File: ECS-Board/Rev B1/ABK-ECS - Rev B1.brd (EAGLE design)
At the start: 100 x 100 mm, 298 parts, among them J1 USB-B-S-RA, J10 FTSH-105-01-L-DV-NOPASTE, J11 22-05-7028-02, J12 RB1-125BAG1A, J13 22-05-7068-06, J14 22-05-7048-04, J15 22-05-7048-04, J16 22-05-7048-04, J2 MSTBA2, J3 22-05-7068-06, J5 22-05-7068-06, J6 22-05-7068-06, J7 22-05-7068-06, J8 22-05-7028-02, J9 FTSH-103-01-L-DV-NOPASTE, SW1 B3FS-1015, SW2 B3FS-1015, T1 MMBT2907ALT3, T10 MMBT2222AL, T11 IRLML5103TRPBF, T12 MMBT2222AL, T13 IRLML5103TRPBF, T14 IRLML5103TRPBF, T15 IRLML5103TRPBF, T16 IRLML5103TRPBF, T17 MMBT2222AL, T18 MMBT2222AL, T19 MMBT2222AL, T2 EXMACHINA-LOGO-NAME, T20 MMBT2222AL, T3 IRLML5103TRPBF, T4 IRLML5103TRPBF, T5 IRLML5103TRPBF, T6 IRLML5103TRPBF, T7 MMBT2222AL, T8 MMBT2222AL, T9 MMBT2222AL, U1 AT24C512C-SSHM-B, U10 SN74LVC2G17DBVR, U2 LPC1768FBD100, U3 LT3686HDDPBF, U4 LT3686HDDPBF, U5 CD4050BD, U6 CD4050BD, U7 DP83848JSQ/NOPB, U9 SN74LVC2G17DBVR, X1 FC-135, X2 ASE-12, X3 3000, X4 ASE_50

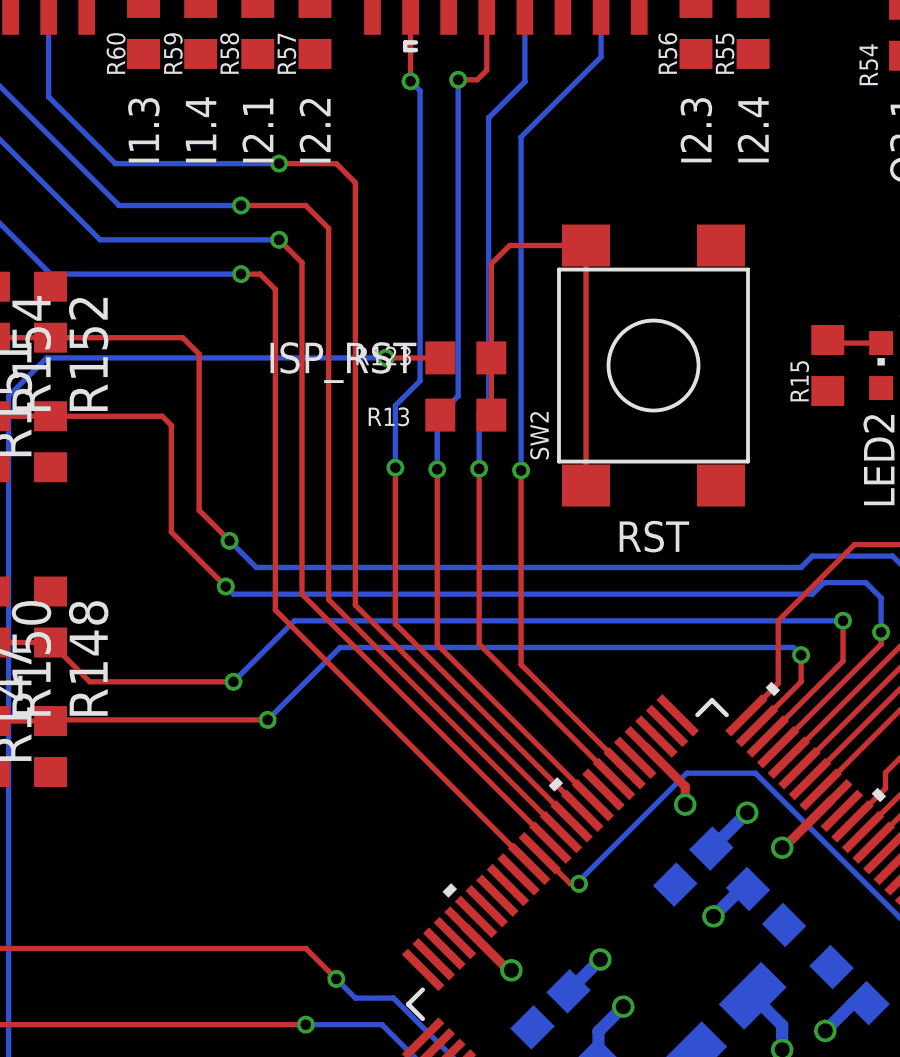
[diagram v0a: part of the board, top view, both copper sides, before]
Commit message: Re-Map MCU output signal
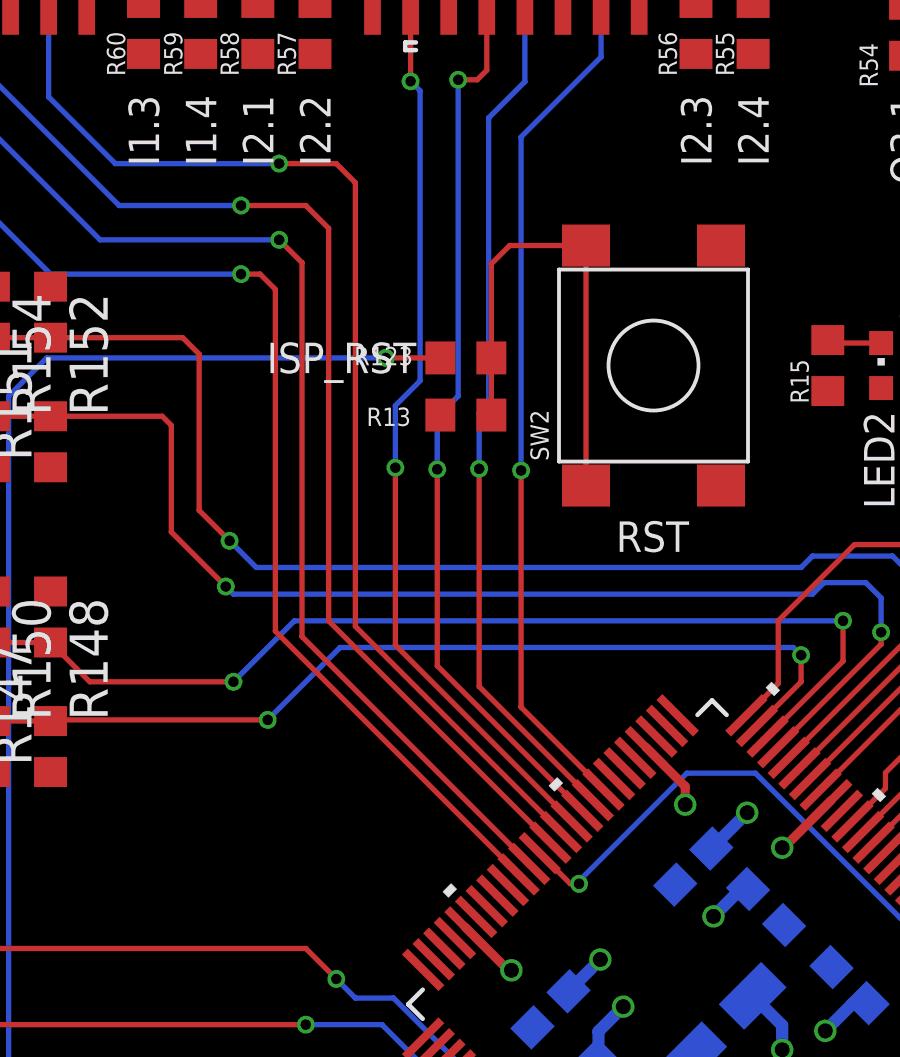
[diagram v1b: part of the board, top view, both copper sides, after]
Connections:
- net INPUT1.1_MCU: now also U2.66; no longer U2.65
- net INPUT1.2_MCU: now also U2.65; no longer U2.63
- net INPUT1.3_MCU: now also U2.63; no longer U2.62
- net INPUT1.4_MCU: now also U2.62; no longer U2.61
- net INPUT2.1_MCU: now also U2.60; no longer U2.59
- net INPUT2.2_MCU: now also U2.61; no longer U2.60
- net INPUT2.3_MCU: now also U2.59; no longer U2.57
- net INPUT2.4_MCU: now also U2.58; no longer U2.56
- net ONBOARD_LED1: now also U2.57
- net ONBOARD_LED2: now also U2.56

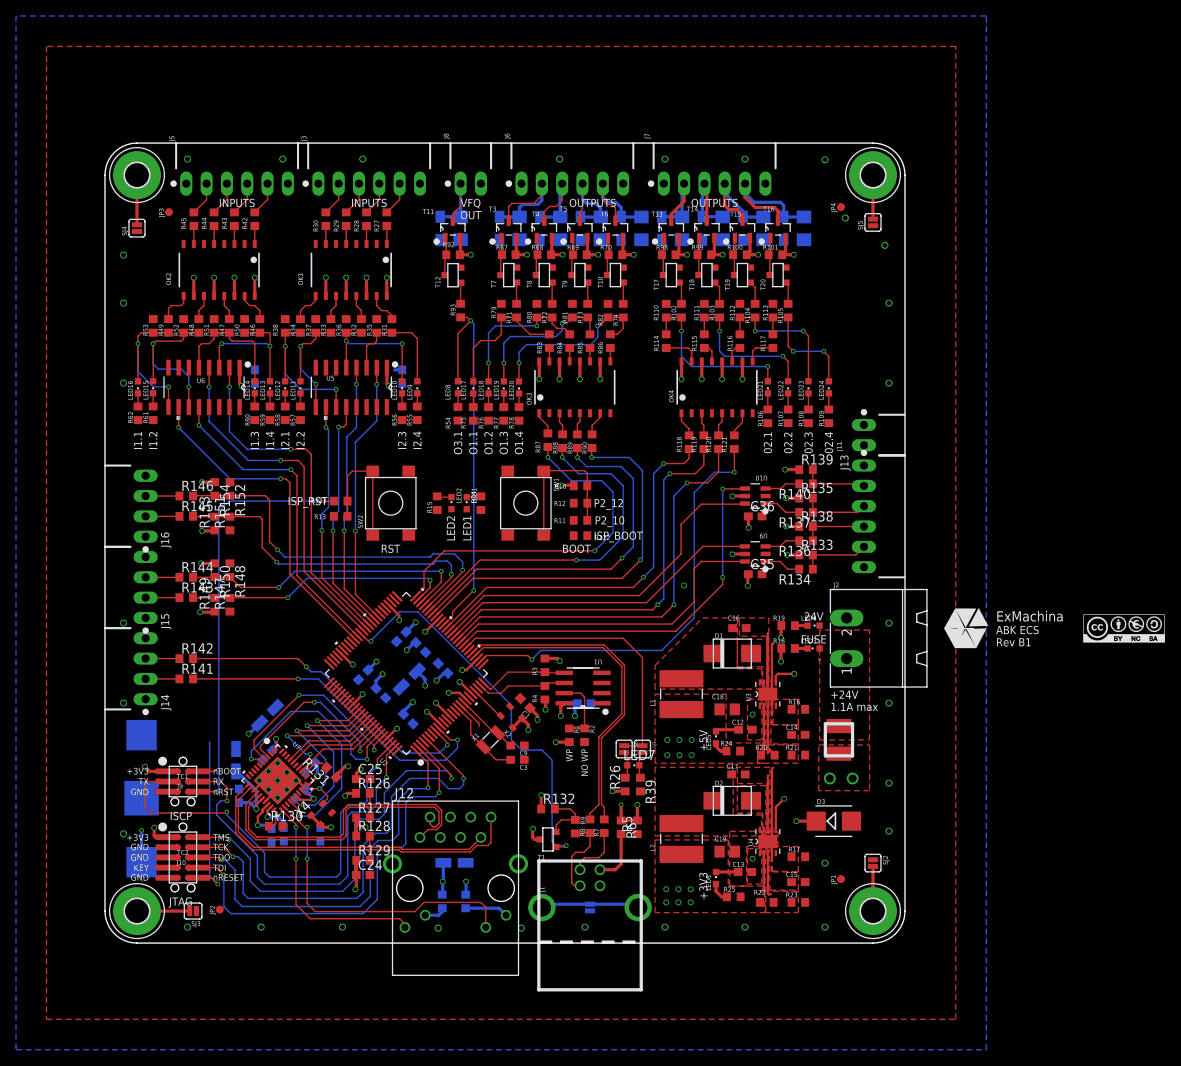
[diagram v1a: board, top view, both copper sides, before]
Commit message: Move RTC battery holder and route VBAT, Boot signals and Leds signals
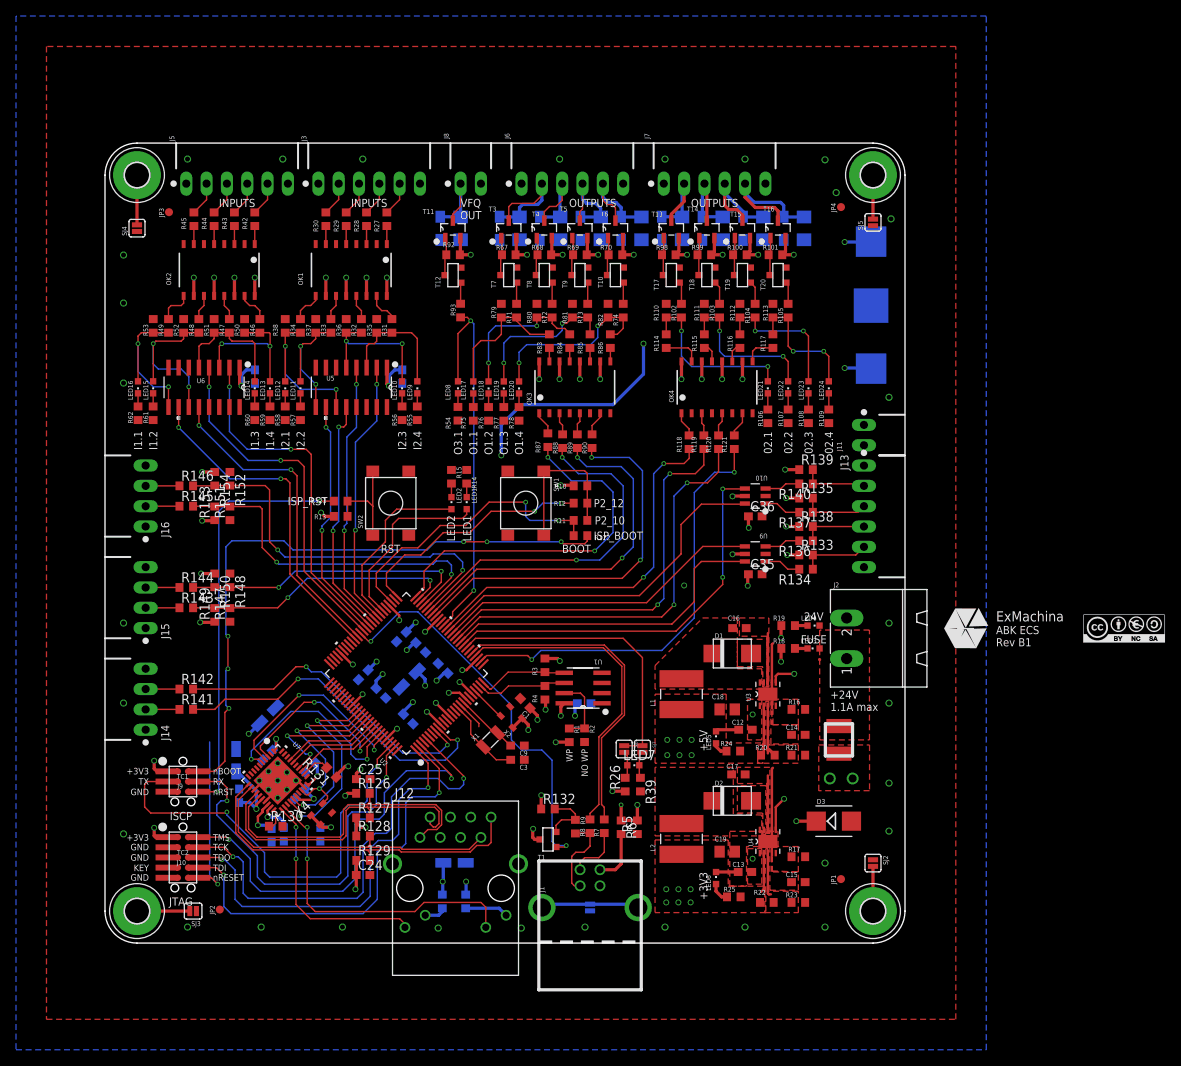
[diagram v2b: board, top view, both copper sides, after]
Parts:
- moved X3 110.0 mm to (95.8, 79.7), turned to 90 degrees
- moved R141 3.81 mm to (10.2, 29.2)
- moved R142 3.81 mm to (10.2, 31.8)
- moved J14 3.81 mm to (5.08, 30.5)
- moved R14 3.75 mm to (45.2, 58.3), turned to 90 degrees
- moved R15 3.75 mm to (43.3, 58.3), turned to 90 degrees
- moved J15 1.27 mm to (5.08, 43.2)
- moved J16 1.27 mm to (5.08, 55.9)
- moved R143 1.27 mm to (10.2, 41.9)
- moved R148 1.27 mm to (15.6, 45.3)
- moved R150 1.27 mm to (13.7, 45.3)
- moved R152 1.27 mm to (15.6, 58.0)
- moved R154 1.27 mm to (13.7, 58.0)
- moved R144 1.27 mm to (10.2, 44.5)
- moved R145 1.27 mm to (10.2, 54.6)
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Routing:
- net VBAT+: track 6.55 -> 113.8 mm, vias 2 -> 5
- net !ISP_BOOT: track 3.87 -> 79.8 mm, vias 0 -> 6
- net BOOT_SELECT_P2_10: track 0.00 -> 36.6 mm, vias 0 -> 2
- net BOOT_SELECT_P2_12: track 0.00 -> 30.5 mm, vias 0 -> 2
- net ONBOARD_LED2: track 0.00 -> 23.1 mm
- net ONBOARD_LED1: track 0.00 -> 22.6 mm
- net +3V3: track 121.3 -> 128.4 mm, vias 56 -> 57
- net !RESET: track 42.3 -> 39.2 mm
- net ADC2: track 42.0 -> 43.5 mm
- net UART_TX: track 48.1 -> 49.3 mm
- net UART_RX: track 43.6 -> 44.9 mm
- net ADC1: track 39.5 -> 40.2 mm
- net I2C_SDA: track 37.3 -> 36.8 mm
- net I2C_SCL: track 33.7 -> 34.3 mm
- net GND: vias 41 -> 40

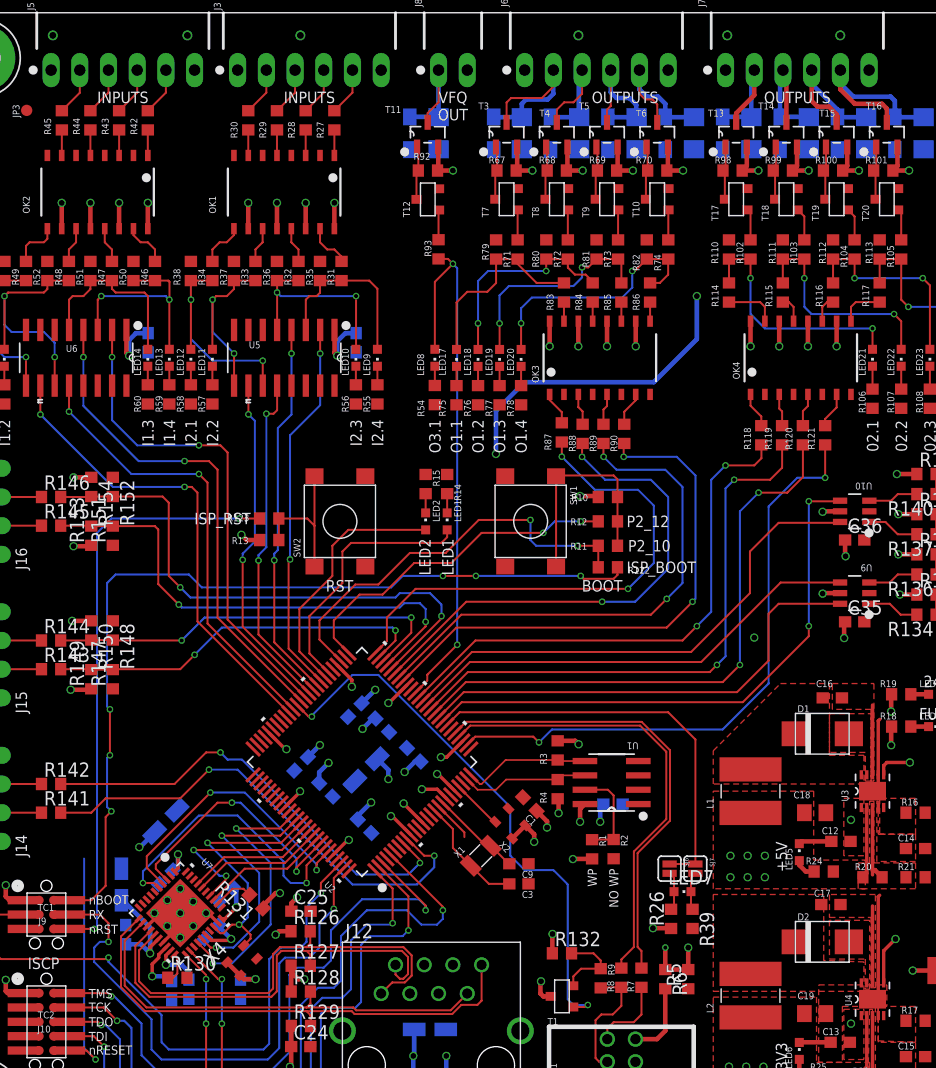
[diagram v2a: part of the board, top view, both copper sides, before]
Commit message: Route Reset and all airwire
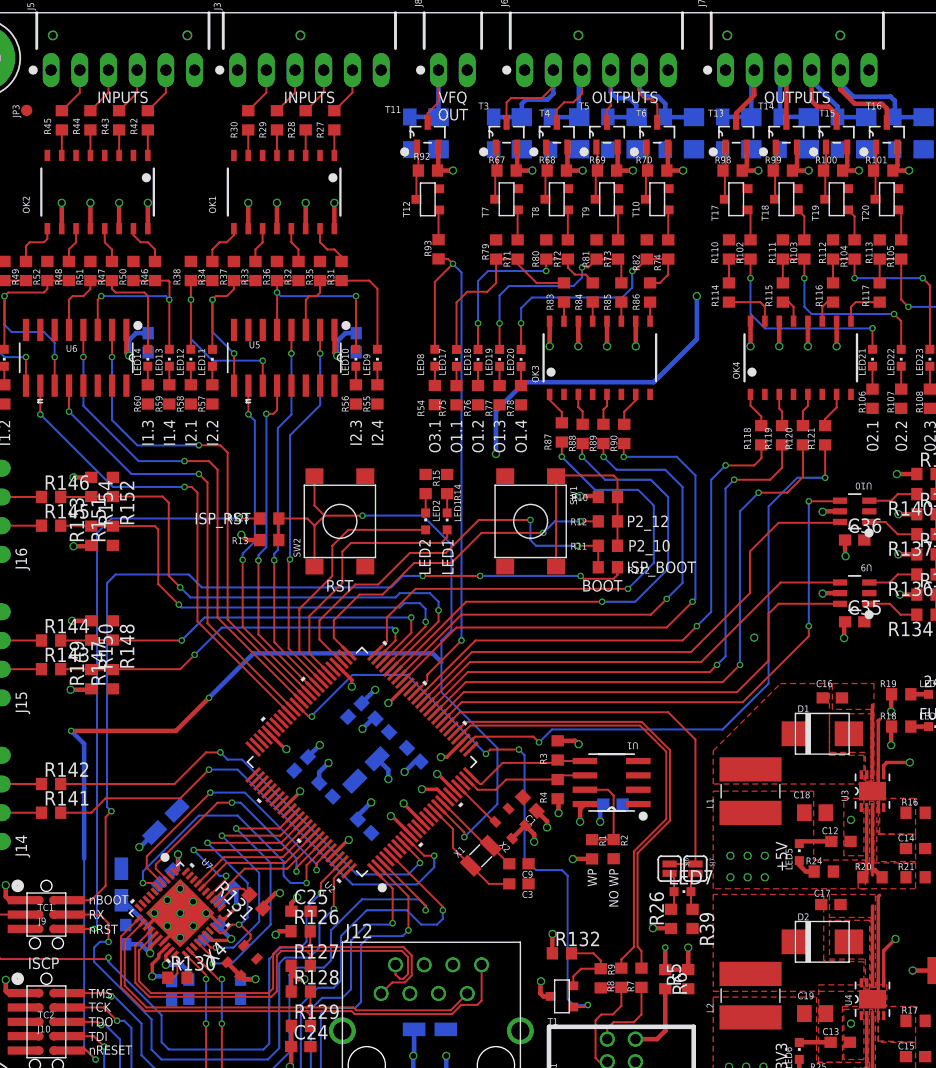
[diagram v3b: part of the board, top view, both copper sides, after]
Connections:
- net ONBOARD_LED1: no longer U2.75
- net ONBOARD_LED2: no longer U2.74
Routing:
- net !RESET: track 39.2 -> 129.4 mm, vias 1 -> 5
- net USB_CONNECT: track 49.7 -> 53.3 mm, vias 2 -> 4
- net !ISP_BOOT: track 79.8 -> 79.6 mm, vias 6 -> 4
